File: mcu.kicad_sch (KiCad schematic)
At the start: 7 parts, among them U1 ATSAMD21G18A-A

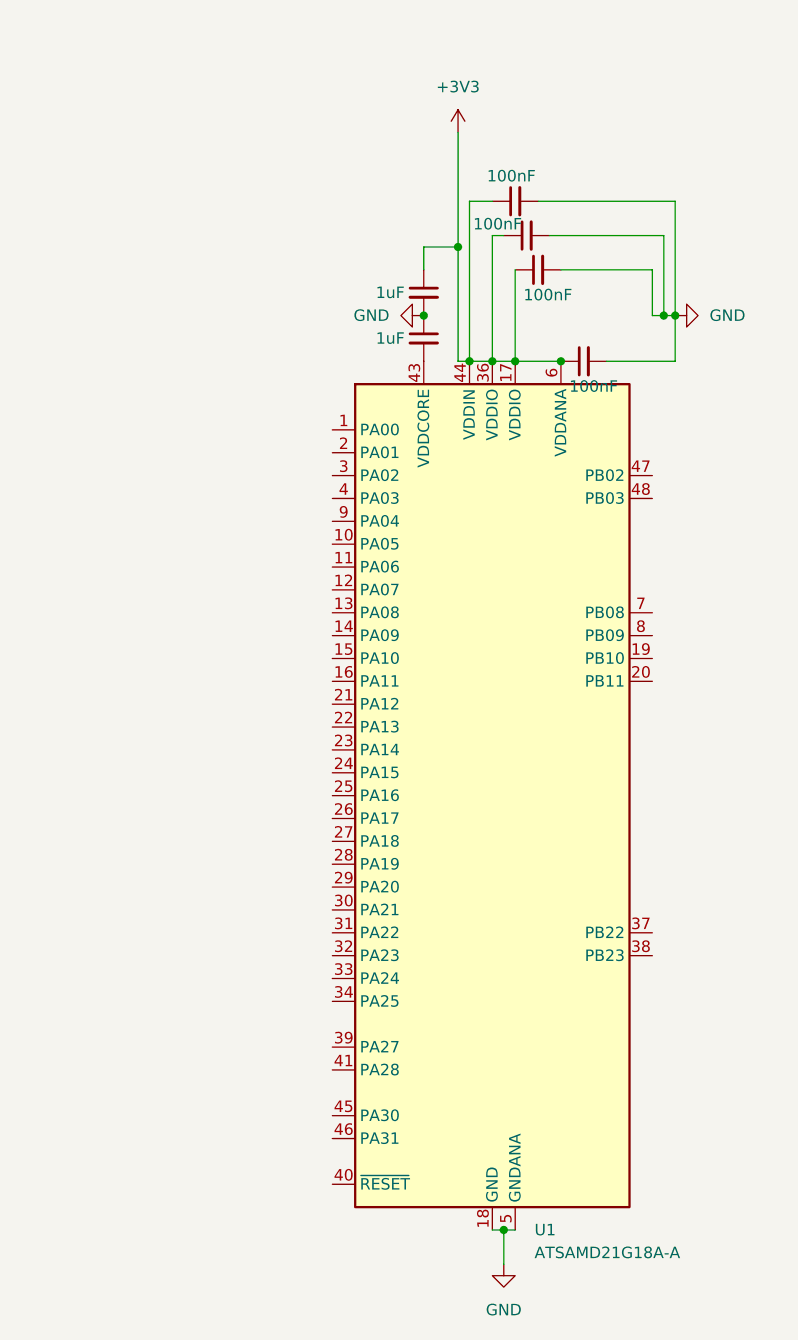
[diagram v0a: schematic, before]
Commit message: imu, motor esc schematics
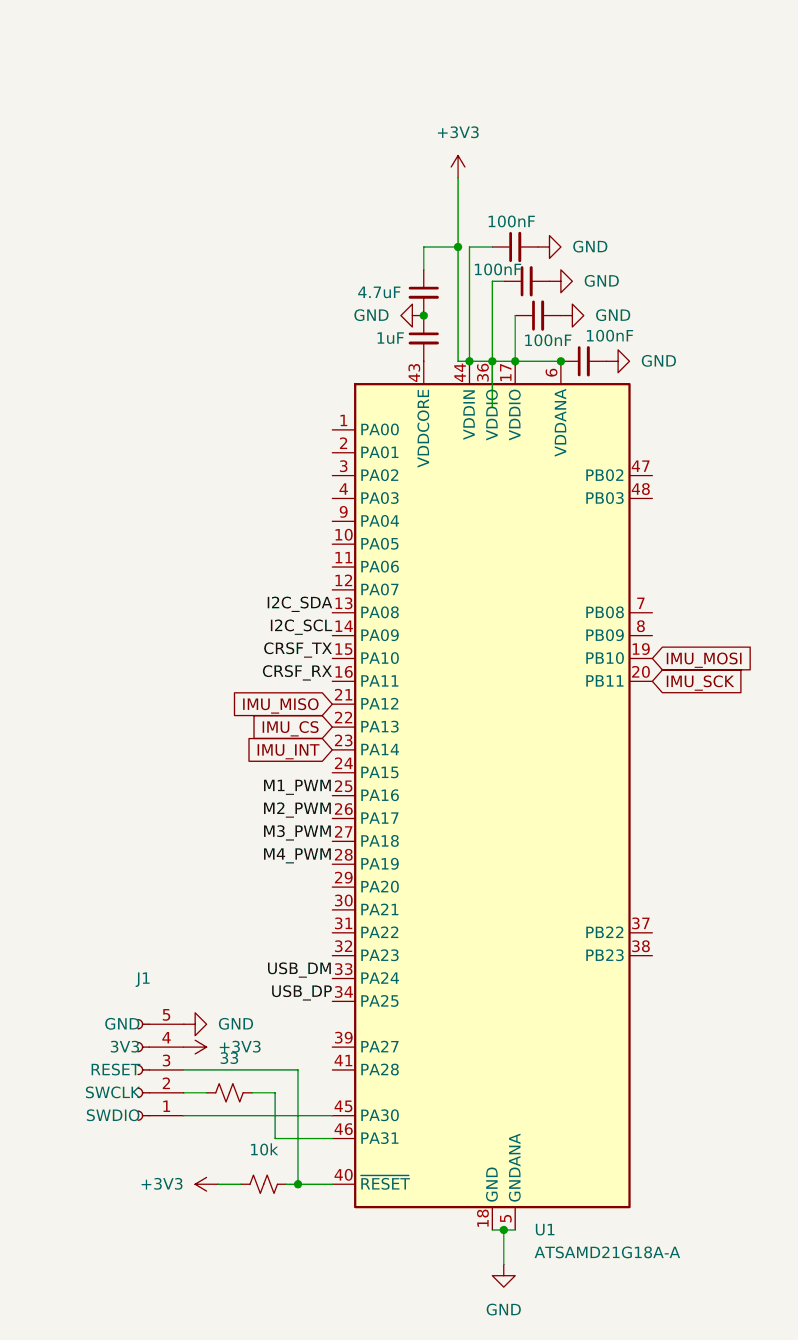
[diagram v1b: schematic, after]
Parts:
- added J1: Conn_01x05_Socket, Connector_PinHeader_2.54mm:PinHeader_1x05_P2.54mm_Vertical, symbol Connector:Conn_01x05_Socket
- added R1: 10k, Resistor_SMD:R_0603_1608Metric_Pad0.98x0.95mm_HandSolder, symbol Device:R_Small_US
- added R2: 33, Resistor_SMD:R_0603_1608Metric_Pad0.98x0.95mm_HandSolder, symbol Device:R_Small_US
- C6: value 1uF -> 4.7uF
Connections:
- net +3V3: now also J1.4 (3V3), R1.1
- net GND: now also J1.5 (GND)
- net I2C_SDA: now reaches U1.13 (PA08)
- net I2C_SCL: now reaches U1.14 (PA09)
- net CRSF_TX: now reaches U1.15 (PA10)
- net CRSF_RX: now reaches U1.16 (PA11)
- net IMU_MOSI: now reaches U1.19 (PB10)
- net IMU_SCK: now reaches U1.20 (PB11)
- net IMU_MISO: now reaches U1.21 (PA12)
- net IMU_CS: now reaches U1.22 (PA13)
- net IMU_INT: now reaches U1.23 (PA14)
- net M1_PWM: now reaches U1.25 (PA16)
- net M2_PWM: now reaches U1.26 (PA17)
- net M3_PWM: now reaches U1.27 (PA18)
- net M4_PWM: now reaches U1.28 (PA19)
- net USB_DM: now reaches U1.33 (PA24)
- net USB_DP: now reaches U1.34 (PA25)
- net at U1.40 (~{RESET}): now also J1.3 (RESET), R1.2
- net at U1.45 (PA30): now also J1.1 (SWDIO)
- net at U1.46 (PA31): now also R2.2
- new net: J1.2 (SWCLK), R2.1

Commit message: more esc schematics, refactoring, root schematic edits
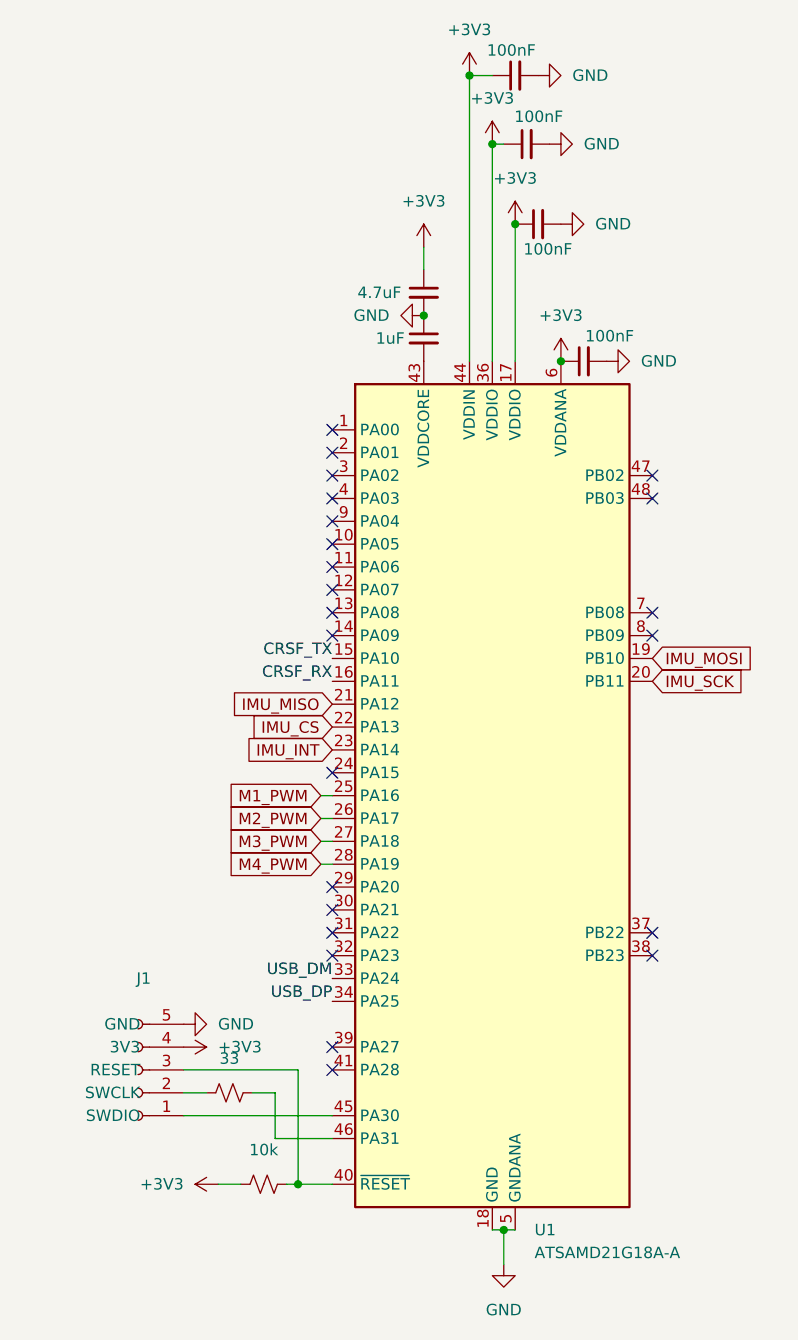
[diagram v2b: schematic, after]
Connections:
- net I2C_SCL: no longer names the net of U1.14 (PA09)
- net I2C_SDA: no longer names the net of U1.13 (PA08)
- no-connect marks 0 -> 23

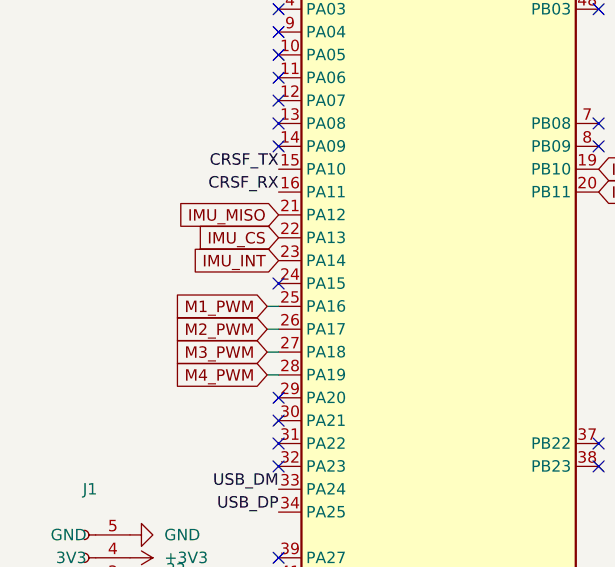
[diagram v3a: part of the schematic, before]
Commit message: A LOT of changes, current state is 2 of 4 ESCs routed, power revamped. \n Board almost done
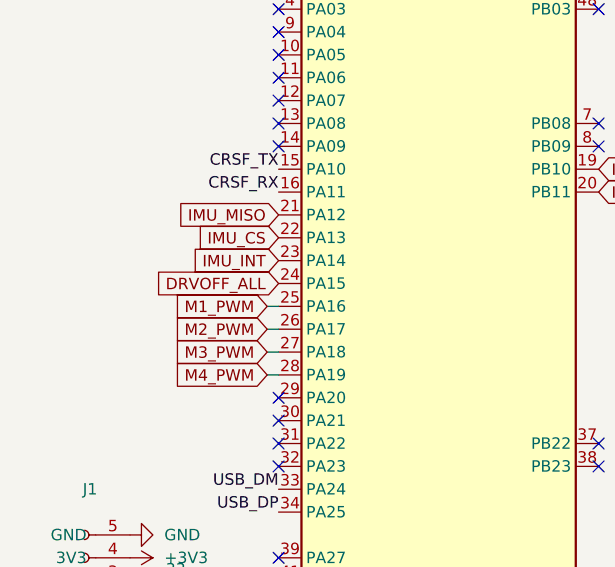
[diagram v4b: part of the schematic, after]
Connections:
- net DRVOFF_ALL: now reaches U1.24 (PA15)
- no-connect marks 23 -> 22
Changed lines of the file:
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@@
-	)
-	(no_connect
-		(at 95.25 130.81)
 	)
 	(no_connect
@@
 			(effects
 				(font
+					(size 1.27 1.27)
+				)
+				(justify right)
+				(hide yes)
+			)
+		)
+	)
+	(global_label "DRVOFF_ALL"
+		(shape input)
+		(at 95.25 130.81 180)
+		(fields_autoplaced yes)
+		(effects
+			(font
+				(size 1.27 1.27)
+			)
+			(justify right)
+		)
+		(property "Intersheetrefs" "${INTERSHEET_REFS}"
+			(at 81.0161 130.81 0)
+			(effects
+				(font

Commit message: done?
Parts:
- added R4: 10k, Resistor_SMD:R_0402_1005Metric_Pad0.72x0.64mm_HandSolder, symbol Device:R_Small_US
- J1: footprint Connector_PinHeader_2.54mm:PinHeader_1x05_P2.54mm_Vertical -> Connector_PinSocket_1.00mm:PinSocket_1x05_P1.00mm_Vertical_SMD_Pin1Left
- R1, R2: footprint Resistor_SMD:R_0603_1608Metric_Pad0.98x0.95mm_HandSolder -> Resistor_SMD:R_0402_1005Metric_Pad0.72x0.64mm_HandSolder
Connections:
- net +3V3: now also R4.2
- net DRVOFF_ALL: now also R4.1
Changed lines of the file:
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@@
+	)
+	(junction
+		(at 80.01 130.81)
+		(diameter 0)
+		(color 0 0 0 0)
 	)
 	(junction
@@
 	(wire
 		(pts
+			(xy 80.01 130.81) (xy 95.25 130.81)
+		)
+		(stroke
+			(width 0)
+			(type default)
+		)
+	)
+	(wire
+		(pts
 			(xy 115.57 181.61) (xy 114.3 181.61)
 		)
@@
 		)
 	)
-	(label "CRSF_RX"
-		(at 95.25 120.65 180)
-		(effects
-			(font
-				(size 1.27 1.27)
-			)
-			(justify right bottom)
-		)
-	)
-	(label "CRSF_TX"
-		(at 95.25 118.11 180)
-		(effects
-			(font
-				(size 1.27 1.27)
-			)
-			(justify right bottom)
+	(wire
+		(pts
+			(xy 76.2 130.81) (xy 80.01 130.81)
+		)
+		(stroke
+			(width 0)
+			(type default)
 		)
 	)
@@
 		)
 	)
+	(global_label "CRSF_RX"
+		(shape input)
+		(at 95.25 120.65 180)
+		(fields_autoplaced yes)
+		(effects
+			(font
+				(size 1.27 1.27)
+			)
+			(justify right)
+		)
+		(property "Intersheetrefs" "${INTERSHEET_REFS}"
+			(at 83.9796 120.65 0)
+			(effects
+				(font
+					(size 1.27 1.27)
+				)
+				(justify right)
+				(hide yes)
+			)
+		)
+	)
 	(global_label "IMU_SCK"
 		(shape input)
@@
 		)
 	)
-	(global_label "DRVOFF_ALL"
+	(global_label "CRSF_TX"
 		(shape input)
-		(at 95.25 130.81 180)
+		(at 95.25 118.11 180)
 		(fields_autoplaced yes)
 		(effects
@@
 		)
 		(property "Intersheetrefs" "${INTERSHEET_REFS}"
-			(at 81.0161 130.81 0)
+			(at 84.282 118.11 0)
+			(effects
+				(font
+					(size 1.27 1.27)
+				)
+				(justify right)
+				(hide yes)
+			)
+		)
+	)
+	(global_label "DRVOFF_ALL"
+		(shape input)
+		(at 76.2 130.81 180)
+		(fields_autoplaced yes)
+		(effects
+			(font
+				(size 1.27 1.27)
+			)
+			(justify right)
+		)
+		(property "Intersheetrefs" "${INTERSHEET_REFS}"
+			(at 61.9661 130.81 0)
 			(effects
 				(font
@@
 		(on_board yes)
 		(dnp no)
-		(fields_autoplaced yes)
 		(property "Reference" "R2"
 			(at 83.82 160.02 90)
@@
 			)
 		)
-		(property "Footprint" "Resistor_SMD:R_0603_1608Metric_Pad0.98x0.95mm_HandSolder"
+		(property "Footprint" "Resistor_SMD:R_0402_1005Metric_Pad0.72x0.64mm_HandSolder"
 			(at 83.82 166.37 0)
 			(effects
@@
 			)
 		)
-		(property "Datasheet" "~"
+		(property "Datasheet" ""
 			(at 83.82 166.37 0)
 			(effects
@@
 			)
 		)
-		(property "Description" "Resistor, small US symbol"
+		(property "Description" ""
 			(at 83.82 166.37 0)
 			(effects
@@
 	)
 	(symbol
+		(lib_id "Device:R_Small_US")
+		(at 80.01 128.27 180)
+		(unit 1)
+		(exclude_from_sim no)
+		(in_bom yes)
+		(on_board yes)
+		(dnp no)
+		(property "Reference" "R4"
+			(at 73.66 128.27 90)
+			(effects
+				(font
+					(size 1.27 1.27)
+				)
+				(hide yes)
+			)
+		)
+		(property "Value" "10k"
+			(at 76.708 128.27 0)
+			(effects
+				(font
+					(size 1.27 1.27)
+				)
+			)
+		)
+		(property "Footprint" "Resistor_SMD:R_0402_1005Metric_Pad0.72x0.64mm_HandSolder"
+			(at 80.01 128.27 0)
+			(effects
+				(font
+					(size 1.27 1.27)
+				)
+				(hide yes)
+			)
+		)
+		(property "Datasheet" ""
+			(at 80.01 128.27 0)
+			(effects
+				(font
+					(size 1.27 1.27)
+				)
+				(hide yes)
+			)
+		)
+		(property "Description" ""
+			(at 80.01 128.27 0)
+			(effects
+				(font
+					(size 1.27 1.27)
+				)
+				(hide yes)
+			)
+		)
+		(pin "2"
+		)
+		(pin "1"
+		)
+		(instances
+			(project "neodrone-v1"
+				(path "/ec430d83-72cd-4950-a197-fb5338d7c552/91a2a763-470d-4a4d-9e8e-b9069d2f4064"
+					(reference "R4")
+					(unit 1)
+				)
+			)
+		)
+	)
+	(symbol
 		(lib_id "power:GND")
 		(at 125.73 85.09 90)
@@
 			)
 		)
-		(property "Footprint" "Connector_PinHeader_2.54mm:PinHeader_1x05_P2.54mm_Vertical"
+		(property "Footprint" "Connector_PinSocket_1.00mm:PinSocket_1x05_P1.00mm_Vertical_SMD_Pin1Left"
 			(at 73.66 163.83 0)
 			(effects
@@
 			)
 		)
-		(property "Footprint" "Resistor_SMD:R_0603_1608Metric_Pad0.98x0.95mm_HandSolder"
+		(property "Footprint" "Resistor_SMD:R_0402_1005Metric_Pad0.72x0.64mm_HandSolder"
 			(at 87.63 176.53 0)
 			(effects
@@
 			)
 		)
-		(property "Datasheet" "~"
+		(property "Datasheet" ""
 			(at 87.63 176.53 0)
 			(effects
@@
 			)
 		)
-		(property "Description" "Resistor, small US symbol"
+		(property "Description" ""
 			(at 87.63 176.53 0)
 			(effects
@@
 					(unit 1)
 				)
+			)
+		)
+	)
+	(symbol
+		(lib_id "power:+3V3")
+		(at 80.01 125.73 0)
+		(unit 1)
+		(exclude_from_sim no)
+		(in_bom yes)
+		(on_board yes)
+		(dnp no)
+		(property "Reference" "#PWR012"
+			(at 80.01 129.54 0)
+			(effects
+				(font
+					(size 1.27 1.27)
+				)
+				(hide yes)
+			)
+		)
+		(property "Value" "+3V3"
+			(at 77.216 121.158 0)
+			(effects
+				(font
+					(size 1.27 1.27)
+				)
+				(justify left)
+			)
+		)
+		(property "Footprint" ""
+			(at 80.01 125.73 0)
+			(effects
+				(font
+					(size 1.27 1.27)
+				)
+				(hide yes)
+			)
+		)
+		(property "Datasheet" ""
+			(at 80.01 125.73 0)
+			(effects
+				(font
+					(size 1.27 1.27)
+				)
+				(hide yes)
+			)
+		)
+		(property "Description" "Power symbol creates a global label with name \"+3V3\""
+			(at 80.01 125.73 0)
+			(effects
+				(font
+					(size 1.27 1.27)
+				)
+				(hide yes)
+			)
+		)
+		(pin "1"
+		)
+		(instances
+			(project "neodrone-v1"
+				(path "/ec430d83-72cd-4950-a197-fb5338d7c552/91a2a763-470d-4a4d-9e8e-b9069d2f4064"
+					(reference "#PWR012")
+					(unit 1)
+				)
